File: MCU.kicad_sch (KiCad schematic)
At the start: 10 parts

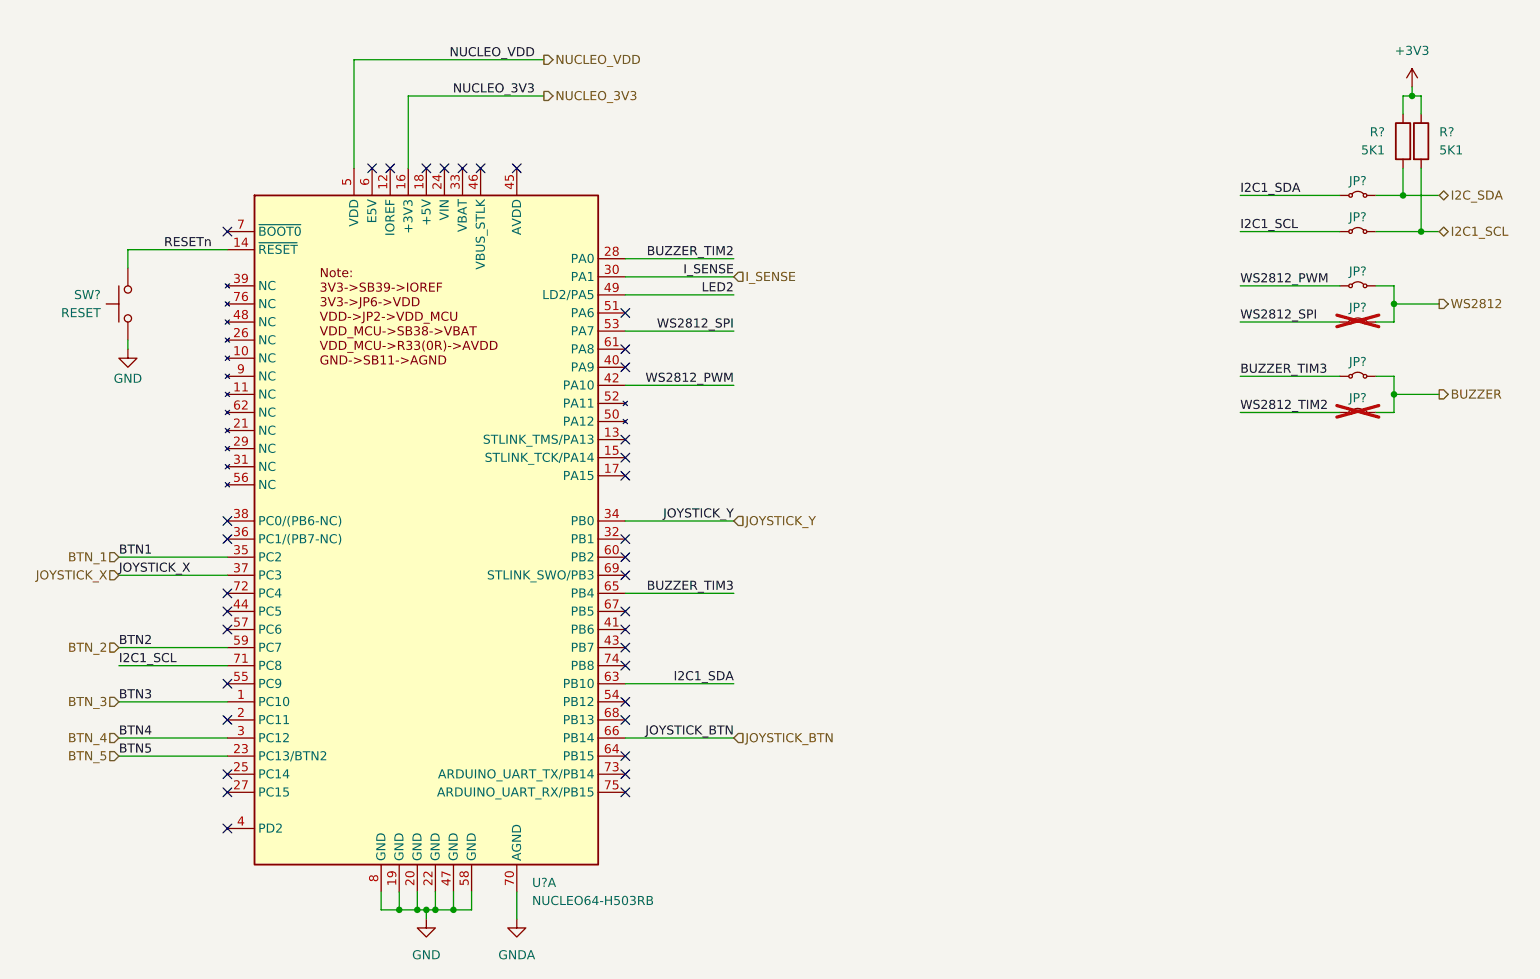
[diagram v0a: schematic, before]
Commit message: Runned ERC for the first time and fixed some errors
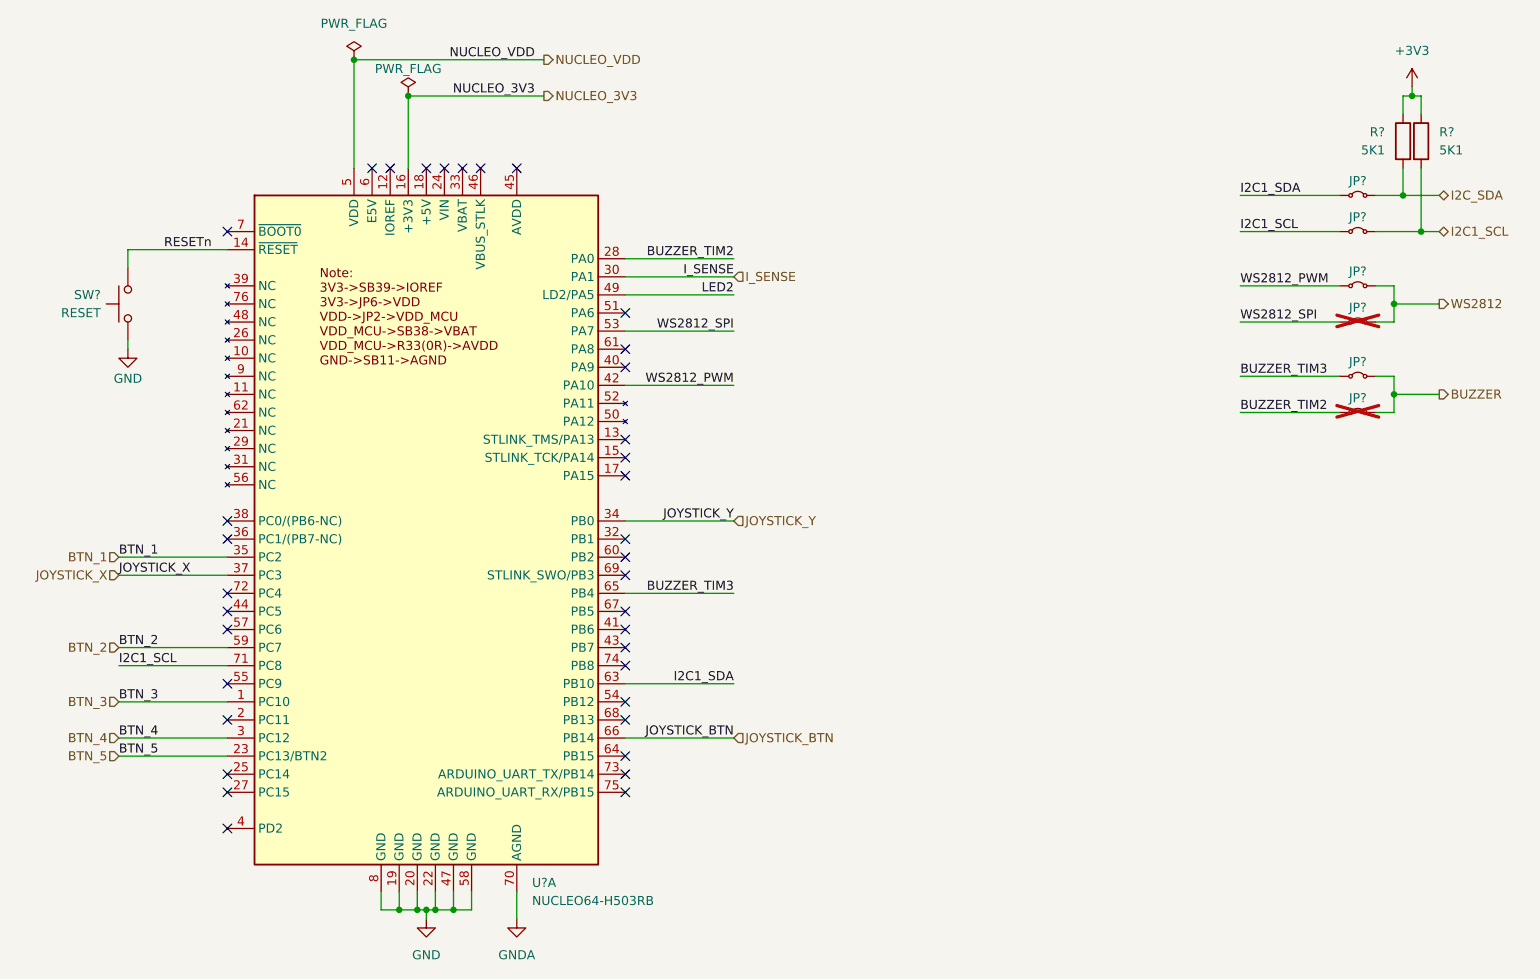
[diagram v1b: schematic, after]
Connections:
- net WS2812_TIM2 is gone; now on net BUZZER_TIM2: JP?.1 (A)
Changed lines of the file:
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@@
+	)
+	(junction
+		(at 90.17 34.29)
+		(diameter 0)
+		(color 0 0 0 0)
+	)
+	(junction
+		(at 82.55 29.21)
+		(diameter 0)
+		(color 0 0 0 0)
 	)
 	(junction
@@
 		)
 	)
-	(label "BTN2"
+	(label "BTN_2"
 		(at 49.53 111.76 0)
 		(effects
@@
 		)
 	)
-	(label "BTN1"
+	(label "BTN_1"
 		(at 49.53 99.06 0)
 		(effects
@@
 		)
 	)
-	(label "BTN5"
+	(label "BTN_5"
 		(at 49.53 127 0)
 		(effects
@@
 		)
 	)
-	(label "BTN4"
+	(label "BTN_4"
 		(at 49.53 124.46 0)
 		(effects
@@
 		)
 	)
-	(label "BTN3"
+	(label "BTN_3"
 		(at 49.53 119.38 0)
 		(effects
@@
 		)
 	)
-	(label "WS2812_TIM2"
+	(label "BUZZER_TIM2"
 		(at 207.01 78.74 0)
 		(effects
@@
 	)
 	(symbol
+		(lib_id "power:PWR_FLAG")
+		(at 82.55 29.21 0)
+		(unit 1)
+		(exclude_from_sim no)
+		(in_bom yes)
+		(on_board yes)
+		(dnp no)
+		(fields_autoplaced yes)
+		(property "Reference" "#FLG?"
+			(at 82.55 27.305 0)
+			(effects
+				(font
+					(size 1.27 1.27)
+				)
+				(hide yes)
+			)
+		)
+		(property "Value" "PWR_FLAG"
+			(at 82.55 24.13 0)
+			(effects
+				(font
+					(size 1.27 1.27)
+				)
+			)
+		)
+		(property "Footprint" ""
+			(at 82.55 29.21 0)
+			(effects
+				(font
+					(size 1.27 1.27)
+				)
+				(hide yes)
+			)
+		)
+		(property "Datasheet" "~"
+			(at 82.55 29.21 0)
+			(effects
+				(font
+					(size 1.27 1.27)
+				)
+				(hide yes)
+			)
+		)
+		(property "Description" "Special symbol for telling ERC where power comes from"
+			(at 82.55 29.21 0)
+			(effects
+				(font
+					(size 1.27 1.27)
+				)
+				(hide yes)
+			)
+		)
+		(pin "1"
+		)
+		(instances
+			(project ""
+				(path "/835b4df9-7d62-45f4-81d2-5a64fbc86f3c/a718e7a0-c449-4532-ac19-5f778084acdd"
+					(reference "#FLG?")
+					(unit 1)
+				)
+			)
+		)
+	)
+	(symbol
 		(lib_id "ProjectMCUs:NUCLEO64-H503RB")
 		(at 92.71 95.25 0)
@@
 		(dnp no)
 		(fields_autoplaced yes)
-		(property "Reference" "#PWR0114"
+		(property "Reference" "#PWR?"
 			(at 231.14 36.83 0)
 			(effects
@@
 		)
 		(instances
-			(project ""
+			(project "Educational-Board_MainBoard"
 				(path "/835b4df9-7d62-45f4-81d2-5a64fbc86f3c/a718e7a0-c449-4532-ac19-5f778084acdd"
-					(reference "#PWR0114")
+					(reference "#PWR?")
 					(unit 1)
 				)
@@
 		(dnp no)
 		(fields_autoplaced yes)
-		(property "Reference" "#PWR0113"
+		(property "Reference" "#PWR?"
 			(at 105.41 156.21 0)
 			(effects
@@
 			(project ""
 				(path "/835b4df9-7d62-45f4-81d2-5a64fbc86f3c/a718e7a0-c449-4532-ac19-5f778084acdd"
-					(reference "#PWR0113")
+					(reference "#PWR?")
 					(unit 1)
 				)
@@
 	)
 	(symbol
+		(lib_id "power:PWR_FLAG")
+		(at 90.17 34.29 0)
+		(unit 1)
+		(exclude_from_sim no)
+		(in_bom yes)
+		(on_board yes)
+		(dnp no)
+		(property "Reference" "#FLG?"
+			(at 90.17 32.385 0)
+			(effects
+				(font
+					(size 1.27 1.27)
+				)
+				(hide yes)
+			)
+		)
+		(property "Value" "PWR_FLAG"
+			(at 90.17 30.48 0)
+			(effects
+				(font
+					(size 1.27 1.27)
+				)
+			)
+		)
+		(property "Footprint" ""
+			(at 90.17 34.29 0)
+			(effects
+				(font
+					(size 1.27 1.27)
+				)
+				(hide yes)
+			)
+		)
+		(property "Datasheet" "~"
+			(at 90.17 34.29 0)
+			(effects
+				(font
+					(size 1.27 1.27)
+				)
+				(hide yes)
+			)
+		)
+		(property "Description" "Special symbol for telling ERC where power comes from"
+			(at 90.17 34.29 0)
+			(effects
+				(font
+					(size 1.27 1.27)
+				)
+				(hide yes)
+			)
+		)
+		(pin "1"
+		)
+		(instances
+			(project ""
+				(path "/835b4df9-7d62-45f4-81d2-5a64fbc86f3c/a718e7a0-c449-4532-ac19-5f778084acdd"
+					(reference "#FLG?")
+					(unit 1)
+				)
+			)
+		)
+	)
+	(symbol
 		(lib_id "power:GND")
 		(at 50.8 69.85 0)
@@
 		(dnp no)
 		(fields_autoplaced yes)
-		(property "Reference" "#PWR0111"
+		(property "Reference" "#PWR?"
 			(at 50.8 76.2 0)
 			(effects
@@
 			(project "Educational-Board_MainBoard"
 				(path "/835b4df9-7d62-45f4-81d2-5a64fbc86f3c/a718e7a0-c449-4532-ac19-5f778084acdd"
-					(reference "#PWR0111")
+					(reference "#PWR?")
 					(unit 1)
 				)
@@
 		(dnp no)
 		(fields_autoplaced yes)
-		(property "Reference" "#PWR0112"
+		(property "Reference" "#PWR?"
 			(at 92.71 156.21 0)
 			(effects
@@
 			(project ""
 				(path "/835b4df9-7d62-45f4-81d2-5a64fbc86f3c/a718e7a0-c449-4532-ac19-5f778084acdd"
-					(reference "#PWR0112")
+					(reference "#PWR?")
 					(unit 1)
 				)

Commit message: Referenced the shematic and started the sourcing part
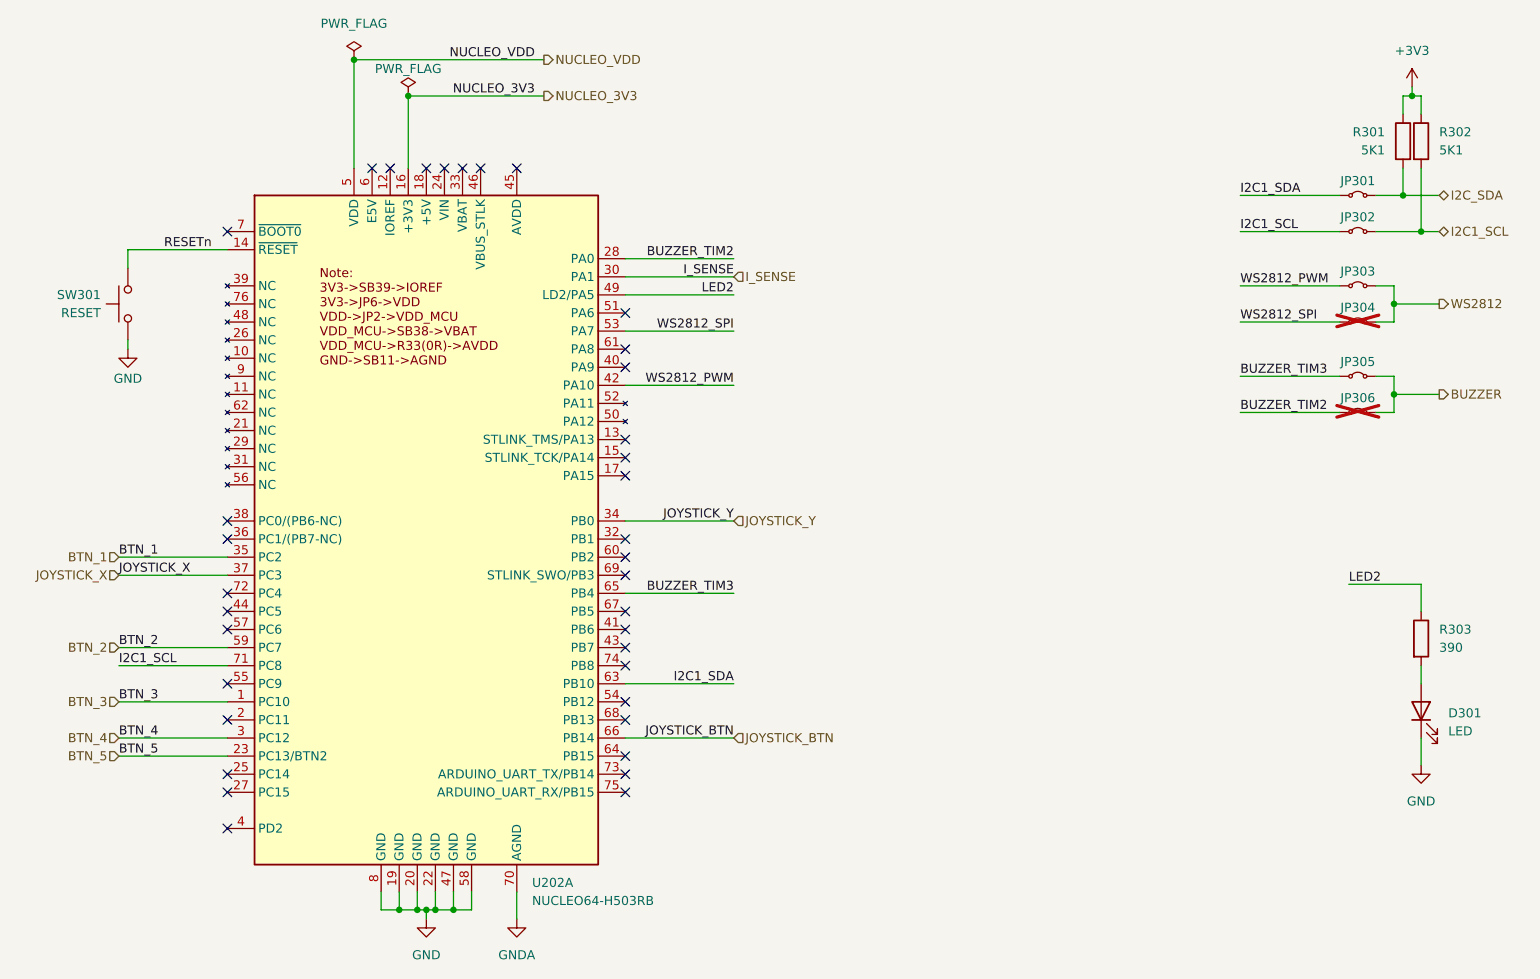
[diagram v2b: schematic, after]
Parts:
- added D301: LED, symbol Device:LED
- added R303: 390, Resistor_SMD:R_0603_1608Metric_Pad0.98x0.95mm_HandSolder, symbol Device:R
- R301, R302: renamed from R?; footprint Resistor_SMD:R_0805_2012Metric_Pad1.20x1.40mm_HandSolder -> Resistor_SMD:R_0603_1608Metric_Pad0.98x0.95mm_HandSolder; LCSC (none) -> C23186
- gave numbers to parts that had none: 8
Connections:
- net GND: now also D301.1 (K)
- net LED2: now also R303.1
- new net: D301.2 (A), R303.2

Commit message: added some lcsc codes, changed reverse voltage protection with a diode
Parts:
- D301: footprint (none) -> LED_SMD:LED_0603_1608Metric; LCSC (none) -> C2290
- JP301, JP302, JP303, JP304, JP305, JP306: footprint (none) -> Resistor_SMD:R_0603_1608Metric_Pad0.98x0.95mm_HandSolder; LCSC (none) -> C21189
- SW301: LCSC (none) -> C455108
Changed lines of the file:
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@@
 			)
 		)
-		(property "Footprint" ""
+		(property "Footprint" "Resistor_SMD:R_0603_1608Metric_Pad0.98x0.95mm_HandSolder"
 			(at 223.52 66.04 0)
 			(effects
@@
 		)
 		(property "Description" "Jumper, 2-pole, small symbol, bridged"
+			(at 223.52 66.04 0)
+			(effects
+				(font
+					(size 1.27 1.27)
+				)
+				(hide yes)
+			)
+		)
+		(property "Sim.Type" ""
+			(at 223.52 66.04 0)
+			(effects
+				(font
+					(size 1.27 1.27)
+				)
+				(hide yes)
+			)
+		)
+		(property "LCSC" "C21189"
 			(at 223.52 66.04 0)
 			(effects
@@
 			)
 		)
+		(property "Sim.Type" ""
+			(at 232.41 40.64 0)
+			(effects
+				(font
+					(size 1.27 1.27)
+				)
+				(hide yes)
+			)
+		)
 		(pin "1"
 		)
@@
 			)
 		)
+		(property "Sim.Type" ""
+			(at 92.71 95.25 0)
+			(effects
+				(font
+					(size 1.27 1.27)
+				)
+				(hide yes)
+			)
+		)
 		(pin "34"
 		)
@@
 			)
 		)
-		(property "Footprint" ""
+		(property "Footprint" "Resistor_SMD:R_0603_1608Metric_Pad0.98x0.95mm_HandSolder"
 			(at 223.52 48.26 0)
 			(effects
@@
 		)
 		(property "Description" "Jumper, 2-pole, small symbol, bridged"
+			(at 223.52 48.26 0)
+			(effects
+				(font
+					(size 1.27 1.27)
+				)
+				(hide yes)
+			)
+		)
+		(property "Sim.Type" ""
+			(at 223.52 48.26 0)
+			(effects
+				(font
+					(size 1.27 1.27)
+				)
+				(hide yes)
+			)
+		)
+		(property "LCSC" "C21189"
 			(at 223.52 48.26 0)
 			(effects
@@
 			)
 		)
-		(property "Footprint" ""
+		(property "Footprint" "Resistor_SMD:R_0603_1608Metric_Pad0.98x0.95mm_HandSolder"
 			(at 223.52 60.96 0)
 			(effects
@@
 		)
 		(property "Description" "Jumper, 2-pole, small symbol, bridged"
+			(at 223.52 60.96 0)
+			(effects
+				(font
+					(size 1.27 1.27)
+				)
+				(hide yes)
+			)
+		)
+		(property "Sim.Type" ""
+			(at 223.52 60.96 0)
+			(effects
+				(font
+					(size 1.27 1.27)
+				)
+				(hide yes)
+			)
+		)
+		(property "LCSC" "C21189"
 			(at 223.52 60.96 0)
 			(effects
@@
 			)
 		)
-		(property "Footprint" ""
+		(property "Footprint" "LED_SMD:LED_0603_1608Metric"
 			(at 232.41 120.65 0)
 			(effects
@@
 		(property "Sim.Pins" "1=K 2=A"
 			(at 232.41 120.65 0)
+			(effects
+				(font
+					(size 1.27 1.27)
+				)
+				(hide yes)
+			)
+		)
+		(property "LCSC" "C2290"
+			(at 232.41 120.65 90)
+			(effects
+				(font
+					(size 1.27 1.27)
+				)
+				(hide yes)
+			)
+		)
+		(property "Sim.Type" ""
+			(at 232.41 120.65 90)
 			(effects
 				(font
@@
 			)
 		)
-		(property "Footprint" ""
+		(property "Footprint" "Resistor_SMD:R_0603_1608Metric_Pad0.98x0.95mm_HandSolder"
 			(at 223.52 78.74 0)
 			(effects
@@
 		)
 		(property "Description" "Jumper, 2-pole, small symbol, bridged"
+			(at 223.52 78.74 0)
+			(effects
+				(font
+					(size 1.27 1.27)
+				)
+				(hide yes)
+			)
+		)
+		(property "Sim.Type" ""
+			(at 223.52 78.74 0)
+			(effects
+				(font
+					(size 1.27 1.27)
+				)
+				(hide yes)
+			)
+		)
+		(property "LCSC" "C21189"
 			(at 223.52 78.74 0)
 			(effects
@@
 			)
 		)
+		(property "Sim.Type" ""
+			(at 50.8 63.5 90)
+			(effects
+				(font
+					(size 1.27 1.27)
+				)
+				(hide yes)
+			)
+		)
+		(property "LCSC" "C455108"
+			(at 50.8 63.5 90)
+			(effects
+				(font
+					(size 1.27 1.27)
+				)
+				(hide yes)
+			)
+		)
 		(pin "1"
 		)
@@
 			)
 		)
+		(property "Sim.Type" ""
+			(at 232.41 110.49 0)
+			(effects
+				(font
+					(size 1.27 1.27)
+				)
+				(hide yes)
+			)
+		)
 		(pin "1"
 		)
@@
 			)
 		)
-		(property "Footprint" ""
+		(property "Footprint" "Resistor_SMD:R_0603_1608Metric_Pad0.98x0.95mm_HandSolder"
 			(at 223.52 53.34 0)
 			(effects
@@
 					(size 1.27 1.27)
 				)
+			)
+		)
+		(property "Sim.Type" ""
+			(at 223.52 53.34 0)
+			(effects
+				(font
+					(size 1.27 1.27)
+				)
+				(hide yes)
+			)
+		)
+		(property "LCSC" "C21189"
+			(at 223.52 53.34 0)
+			(effects
+				(font
+					(size 1.27 1.27)
+				)
+				(hide yes)
 			)
 		)
@@
 			)
 		)
+		(property "Sim.Type" ""
+			(at 229.87 40.64 0)
+			(effects
+				(font
+					(size 1.27 1.27)
+				)
+				(hide yes)
+			)
+		)
 		(pin "1"
 		)
@@
 			)
 		)
-		(property "Footprint" ""
+		(property "Footprint" "Resistor_SMD:R_0603_1608Metric_Pad0.98x0.95mm_HandSolder"
 			(at 223.52 73.66 0)
 			(effects
@@
 			(at 223.52 73.66 0)
 			(effects
+				(font
+					(size 1.27 1.27)
+				)
+				(hide yes)
+			)
+		)
+		(property "Sim.Type" ""
+			(at 223.52 73.66 0)
+			(effects
+				(font
+					(size 1.27 1.27)
+				)
+				(hide yes)
+			)
+		)
+		(property "LCSC" "C21189"
+			(at 223.52 73.66 0)
+			(effects

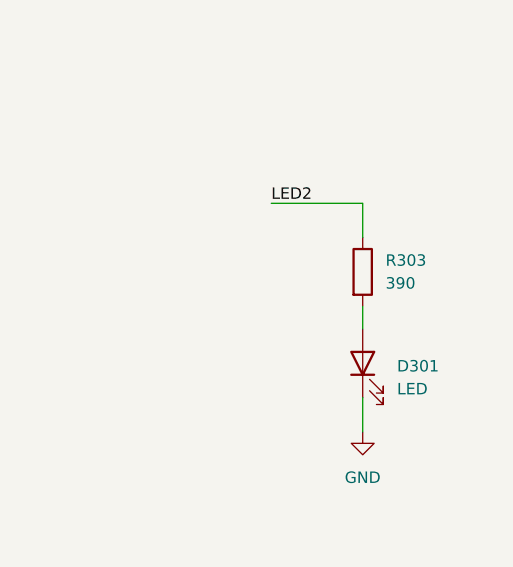
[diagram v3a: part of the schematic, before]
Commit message: added some lcsc PN, and uniformed some resistors values to reduce BOM count
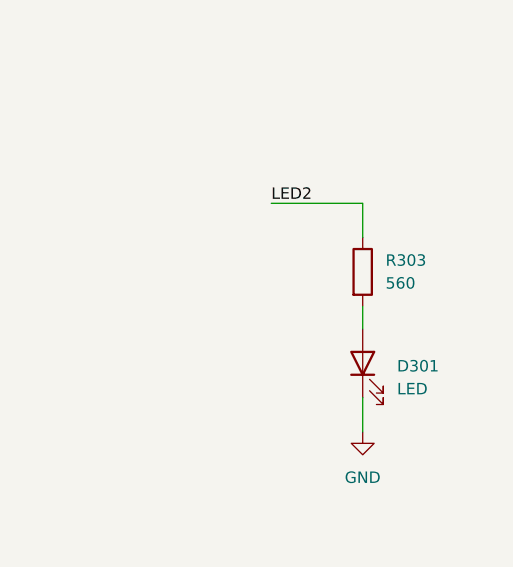
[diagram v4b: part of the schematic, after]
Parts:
- R303: value 390 -> 560; LCSC C23151 -> C23204
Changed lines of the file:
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@@
 			)
 		)
-		(property "Value" "390"
+		(property "Value" "560"
 			(at 234.95 111.7599 0)
 			(effects
@@
 			)
 		)
-		(property "LCSC" "C23151"
+		(property "LCSC" "C23204"
 			(at 232.41 110.49 0)
 			(effects

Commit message: Started the checking of the components
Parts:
- D301, JP301, JP302, JP303, JP304, JP305, JP306, R301, R302, R303: Checked (none) -> OK
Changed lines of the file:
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@@
+			)
+		)
+		(property "Checked" "OK"
+			(at 223.52 66.04 0)
+			(effects
+				(font
+					(size 1.27 1.27)
+				)
+				(hide yes)
 			)
 		)
@@
 			)
 		)
+		(property "Checked" "OK"
+			(at 232.41 40.64 0)
+			(effects
+				(font
+					(size 1.27 1.27)
+				)
+				(hide yes)
+			)
+		)
 		(pin "1"
 		)
@@
 			)
 		)
+		(property "Checked" ""
+			(at 92.71 95.25 0)
+			(effects
+				(font
+					(size 1.27 1.27)
+				)
+				(hide yes)
+			)
+		)
 		(pin "34"
 		)
@@
 			)
 		)
+		(property "Checked" "OK"
+			(at 223.52 48.26 0)
+			(effects
+				(font
+					(size 1.27 1.27)
+				)
+				(hide yes)
+			)
+		)
 		(pin "1"
 		)
@@
 		)
 		(property "LCSC" "C21189"
+			(at 223.52 60.96 0)
+			(effects
+				(font
+					(size 1.27 1.27)
+				)
+				(hide yes)
+			)
+		)
+		(property "Checked" "OK"
 			(at 223.52 60.96 0)
 			(effects
@@
 			)
 		)
+		(property "Checked" "OK"
+			(at 232.41 120.65 90)
+			(effects
+				(font
+					(size 1.27 1.27)
+				)
+				(hide yes)
+			)
+		)
 		(pin "2"
 		)
@@
 		)
 		(property "LCSC" "C21189"
+			(at 223.52 78.74 0)
+			(effects
+				(font
+					(size 1.27 1.27)
+				)
+				(hide yes)
+			)
+		)
+		(property "Checked" "OK"
 			(at 223.52 78.74 0)
 			(effects
@@
 			)
 		)
+		(property "Checked" ""
+			(at 50.8 63.5 90)
+			(effects
+				(font
+					(size 1.27 1.27)
+				)
+				(hide yes)
+			)
+		)
 		(pin "1"
 		)
@@
 			)
 		)
+		(property "Checked" "OK"
+			(at 232.41 110.49 0)
+			(effects
+				(font
+					(size 1.27 1.27)
+				)
+				(hide yes)
+			)
+		)
 		(pin "1"
 		)
@@
 			)
 		)
+		(property "Checked" "OK"
+			(at 223.52 53.34 0)
+			(effects
+				(font
+					(size 1.27 1.27)
+				)
+				(hide yes)
+			)
+		)
 		(pin "1"
 		)
@@
 			)
 		)
+		(property "Checked" "OK"
+			(at 229.87 40.64 0)
+			(effects
+				(font
+					(size 1.27 1.27)
+				)
+				(hide yes)
+			)
+		)
 		(pin "1"
 		)
@@
 			(at 223.52 73.66 0)
 			(effects
+				(font
+					(size 1.27 1.27)
+				)
+				(hide yes)
+			)
+		)
+		(property "Checked" "OK"
+			(at 223.52 73.66 0)
+			(effects
